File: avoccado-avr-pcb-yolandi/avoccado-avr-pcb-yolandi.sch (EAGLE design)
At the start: 36 parts, among them Q1 16MHz

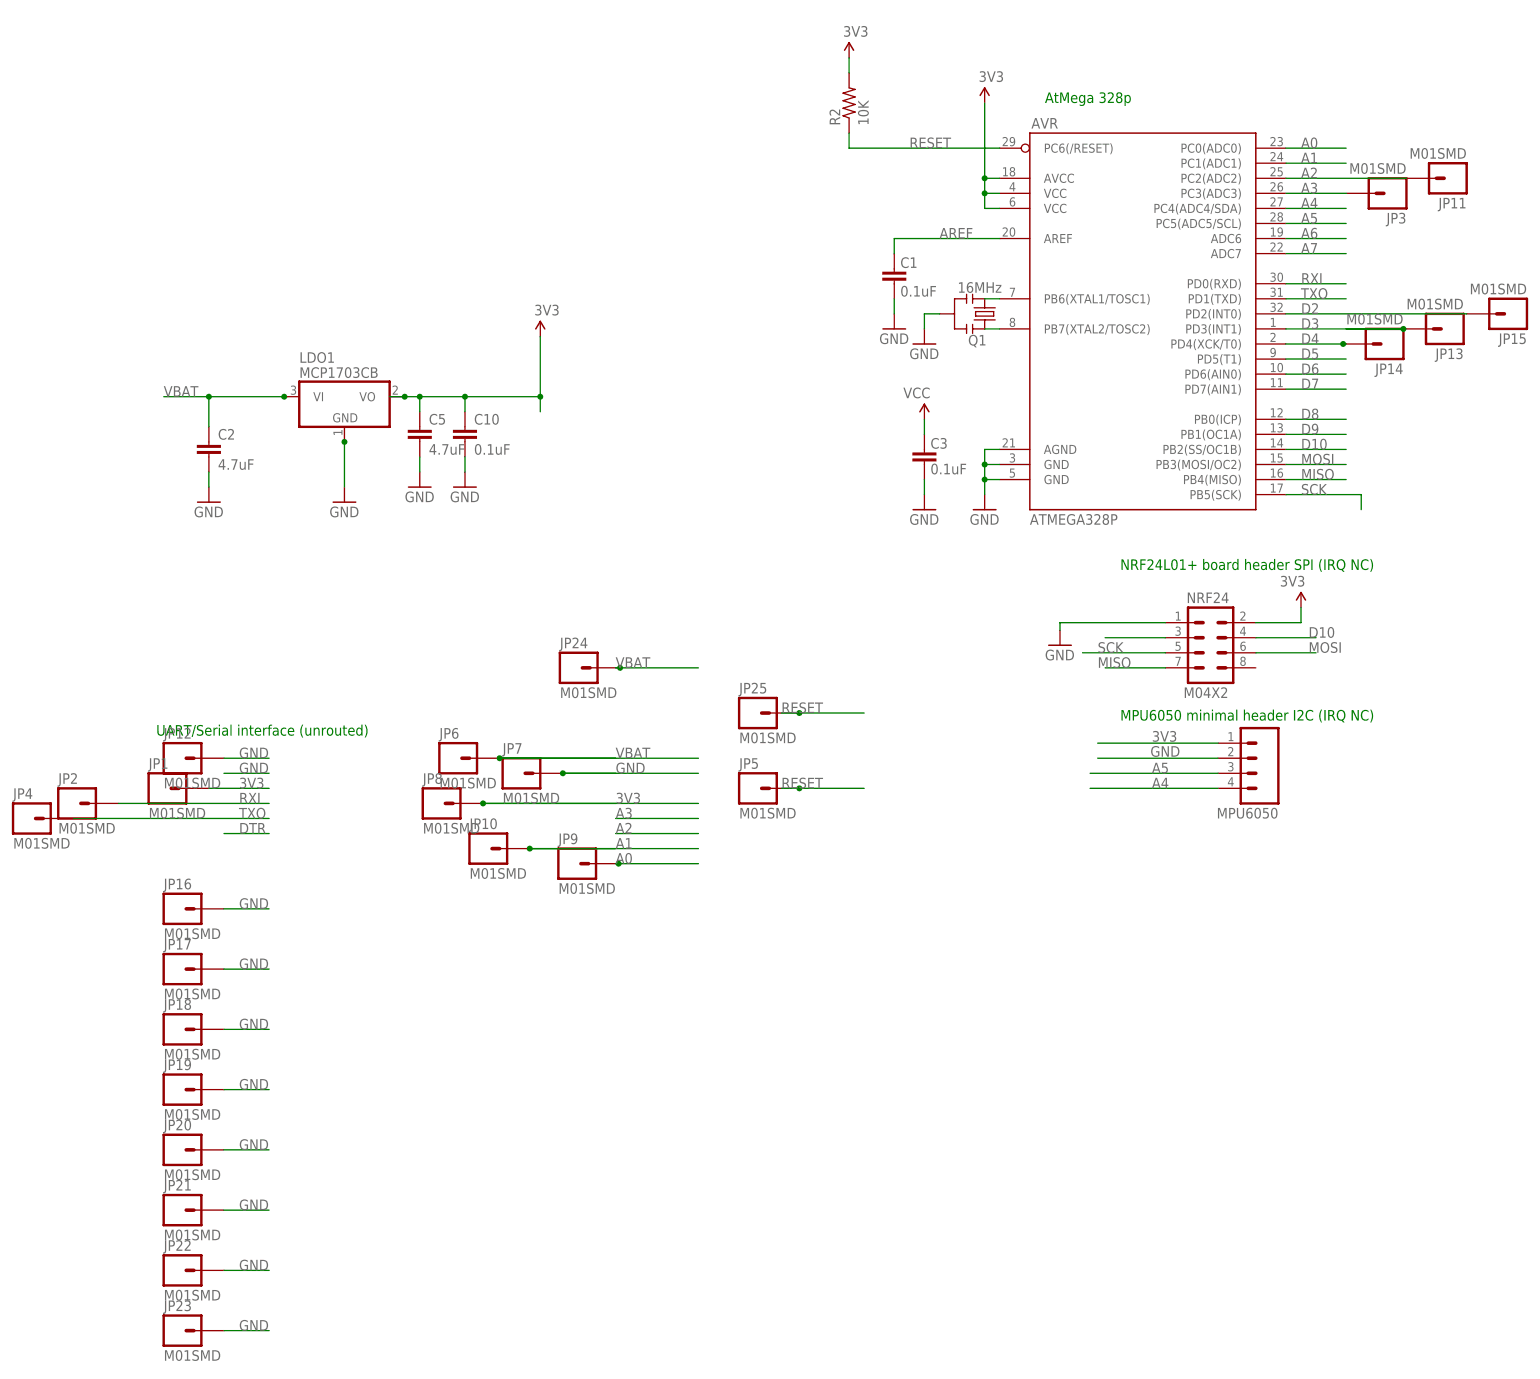
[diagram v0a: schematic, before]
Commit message: start new 1 sq inch PCB fork 'yolandi'
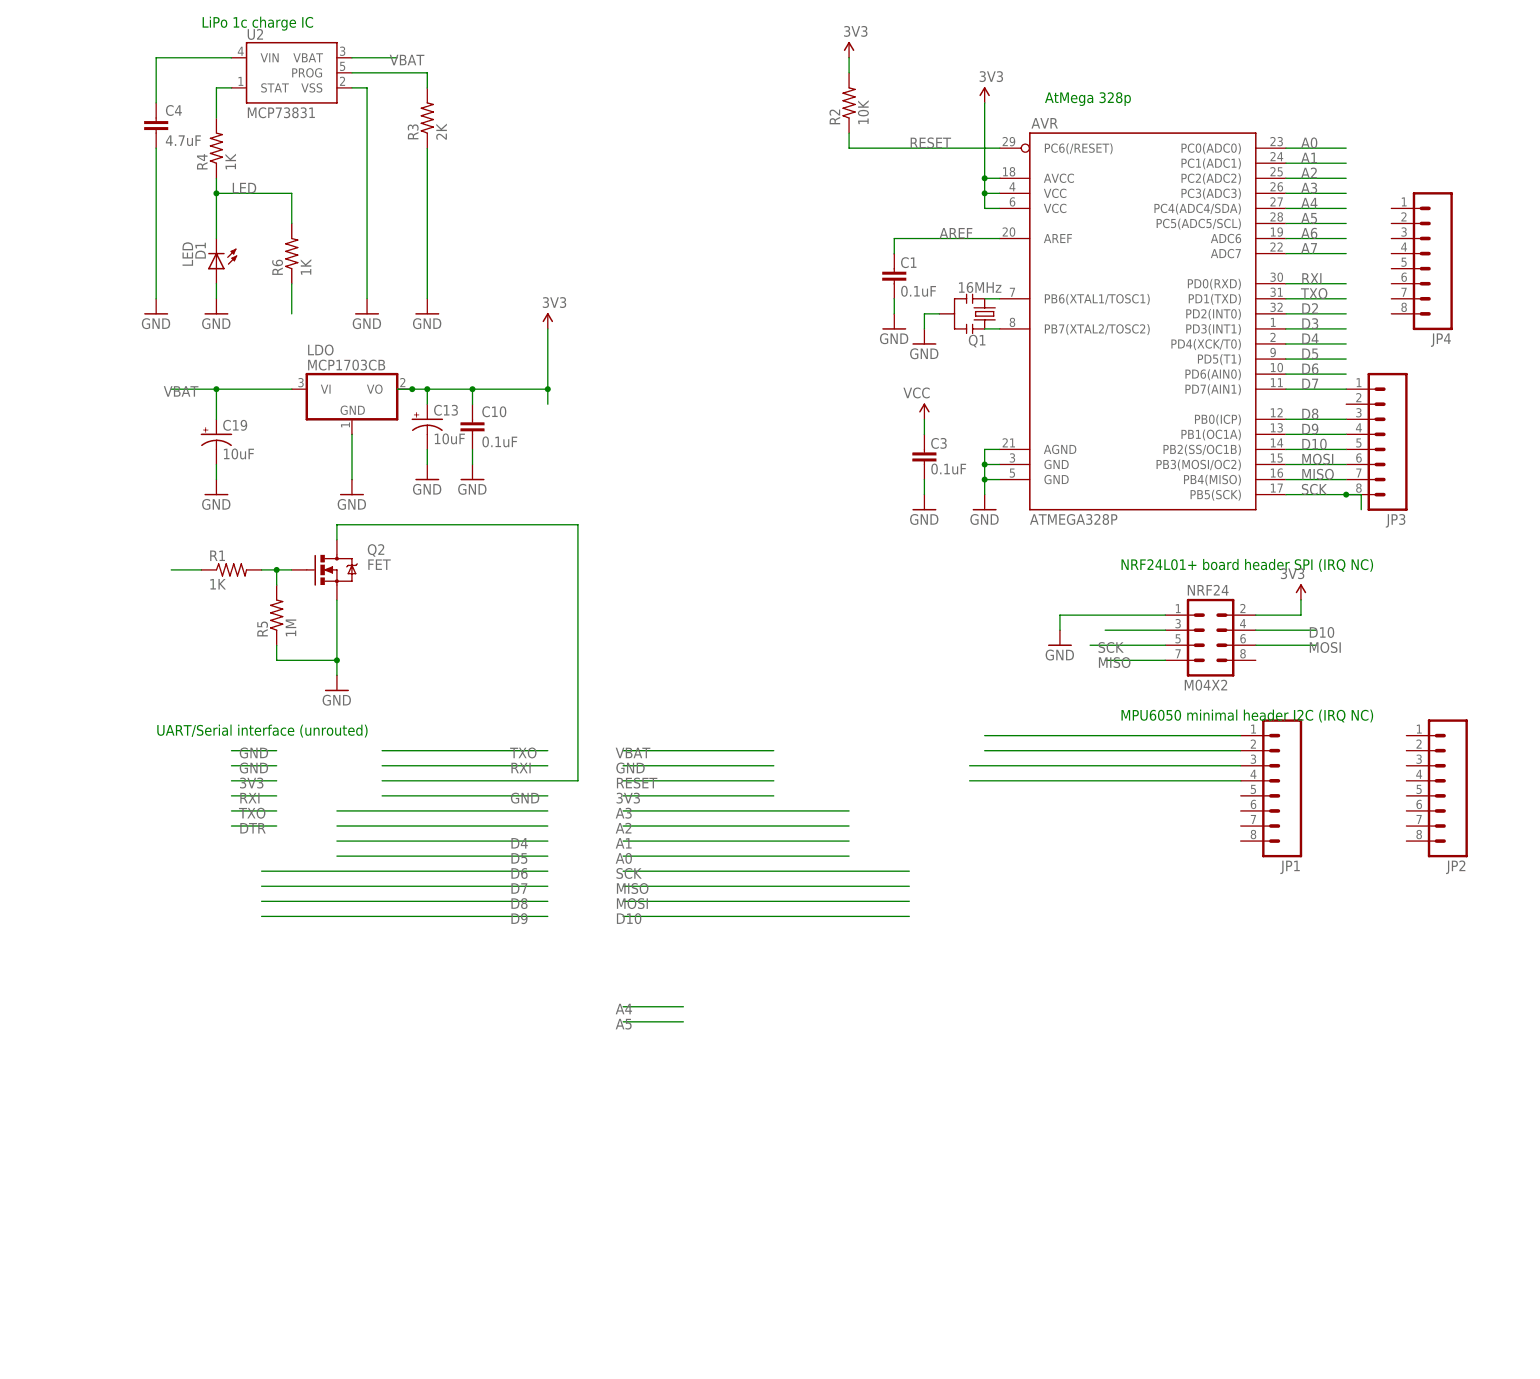
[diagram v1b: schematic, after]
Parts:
- removed C2, C5: 4.7uF, SparkFun-Capacitors:4.7UF-6.3V-10%(0603)0603
- removed JP10, JP11, JP12, JP13, JP14, JP15, JP16, JP17, JP18, JP19, JP20, JP21, JP22, JP23, JP24, JP25, JP5, JP6, JP7, JP8, JP9: M01SMD, SparkFun-Connectors:M01SMD
- removed LDO1: MCP1703CB, linear:MCP1703CB
- removed MPU6050: (no value), SparkFun-Connectors:M041X04_NO_SILK
- added C13, C19: 10uF, SparkFun:CAP_POL1206
- added C4: 4.7uF, SparkFun-Capacitors:4.7UF-6.3V-10%(0603)0603
- added D1: LED, SparkFun:LED0603
- added LDO: MCP1703CB, linear:MCP1703CB
- added Q2: FET, SparkFun-DiscreteSemi:MOSFET-NCHANNEL2N7002PW
- added R1, R4, R6: 1K, SparkFun-Resistors:RESISTOR0603
- added R3: 2K, SparkFun-Resistors:RESISTOR0603
- added R5: 1M, SparkFun-Resistors:RESISTOR0603
- added U2: MCP73831, SparkFun:MCP73831
- JP1, JP2, JP3, JP4: value M01SMD -> (none); device SparkFun-Connectors:M01SMD -> SparkFun-Connectors:M08NO_SILK
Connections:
- new net BUS: C4.1, U2.VIN
- new net LED: D1.C, R4.1, R6.2
- new net N$3: R3.2, U2.PROG
- new net N$4: R4.2, U2.STAT
- new net N$5: R6.1
- new net N$6: Q2.G, R1.2, R5.2
- new net VIBR: Q2.D
- net 3V3: now also C13.+, LDO.VO; no longer C5.1, JP8.1, LDO1.VO, MPU6050.1
- net A0: no longer JP9.1
- net A1: no longer JP10.1
- net A2: no longer JP11.1
- net A3: no longer JP3.1
- net A4: now also JP1.4; no longer MPU6050.4
- net A5: now also JP1.3; no longer MPU6050.3
- net D10: now also JP3.5
- net D2: no longer JP15.1
- net D3: now also R1.1; no longer JP13.1
- net D4: no longer JP14.1
- net D7: now also JP3.1
- net D8: now also JP3.3
- net D9: now also JP3.4
- net GND: now also C13.-, C19.-, C4.2, D1.A, JP1.2, LDO.GND, Q2.S, R3.1, R5.1, U2.VSS; no longer C2.2, C5.2, JP12.1, JP16.1, JP17.1, JP18.1, JP19.1, JP20.1, JP21.1, JP22.1, JP23.1, JP7.1, LDO1.GND, MPU6050.2
- net MISO: now also JP3.7
- net MOSI: now also JP3.6
- net RESET: no longer JP25.1, JP5.1
- net RXI: no longer JP2.1
- net SCK: now also JP3.8
- net TXO: no longer JP4.1
- net VBAT: now also C19.+, LDO.VI, U2.VBAT; no longer C2.1, JP24.1, JP6.1, LDO1.VI
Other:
- note added: "LiPo 1c charge IC"
- moved on the sheet: C10, NRF24

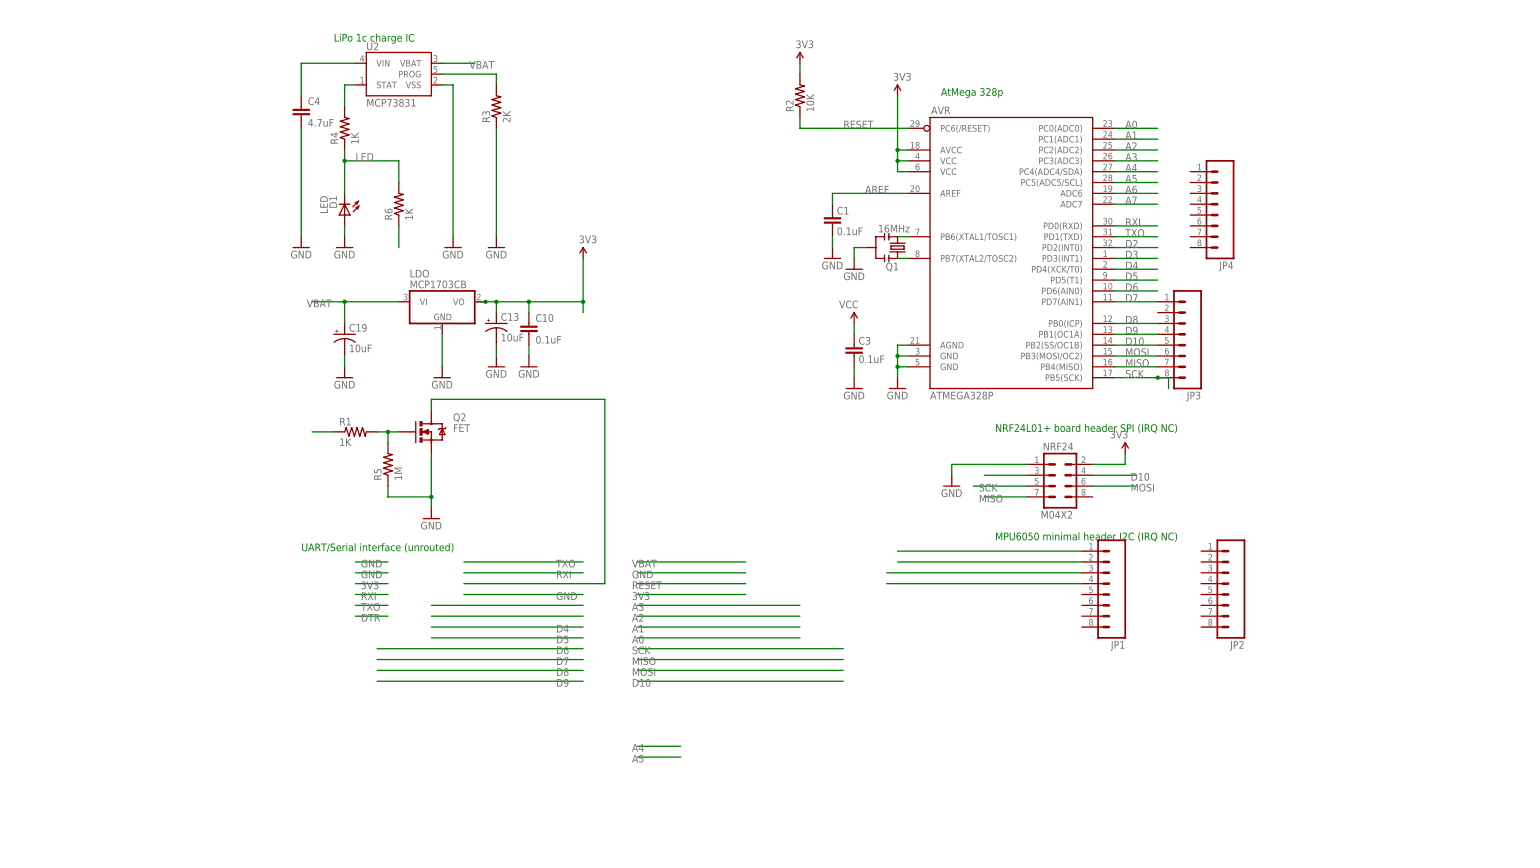
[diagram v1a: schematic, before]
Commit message: routing yolandi
added DTR-reset latch circuit with 0.1uF C
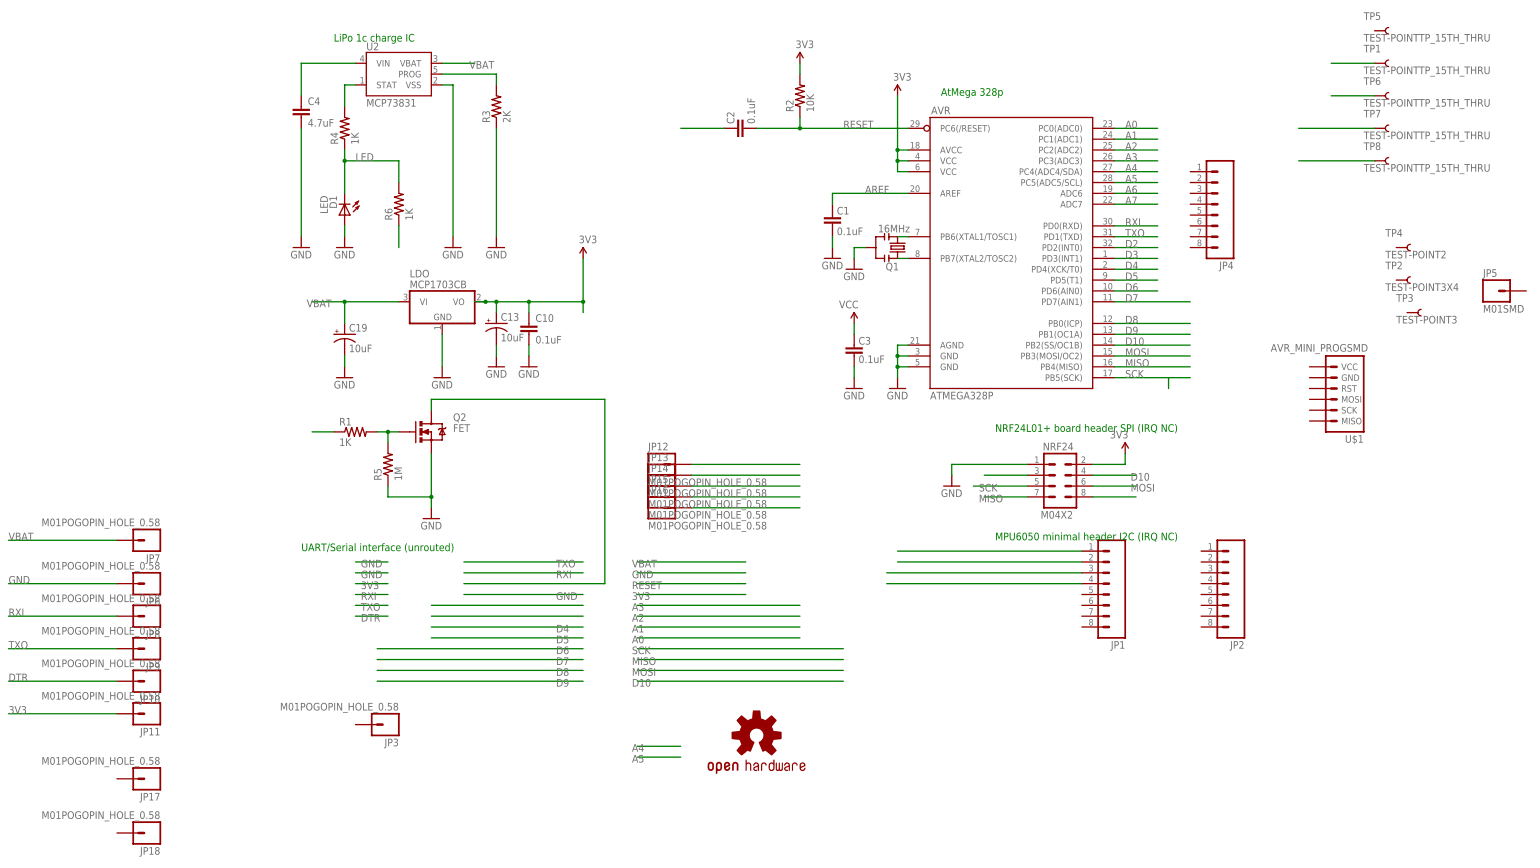
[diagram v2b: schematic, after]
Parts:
- added C2: 0.1uF, SparkFun:CAP0402
- added JP10, JP11, JP12, JP13, JP14, JP15, JP16, JP17, JP18, JP6, JP7, JP8, JP9: M01POGOPIN_HOLE_0.58, SparkFun-Connectors:M01POGOPIN_HOLE_0.58
- added JP5: M01SMD, SparkFun-Connectors:M01SMD
- added LOGO1: OSHW-LOGOS, SparkFun-Aesthetics:OSHW-LOGOS
- added TP1, TP5, TP6, TP7, TP8: TEST-POINTTP_15TH_THRU, SparkFun-Passives:TEST-POINTTP_15TH_THRU
- added TP2: TEST-POINT3X4, SparkFun-Passives:TEST-POINT3X4
- added TP3: TEST-POINT3, SparkFun-Passives:TEST-POINT3
- added TP4: TEST-POINT2, SparkFun-Passives:TEST-POINT2
- added U$1: AVR_MINI_PROGSMD, SparkFun-Connectors:AVR_MINI_PROGSMD
- JP3: value (none) -> M01POGOPIN_HOLE_0.58; device SparkFun-Connectors:M08NO_SILK -> SparkFun-Connectors:M01POGOPIN_HOLE_0.58
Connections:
- net BUS renamed 5V
- net N$3 renamed CHG-PROG
- net N$4 renamed SOC
- removed net N$5: R6.1
- new net DTR: C2.2, JP10.1
- net 3V3: now also JP11.1, JP16.1
- net A7: now also NRF24.8
- net D10: no longer JP3.5
- net D4: now also R6.1
- net D5: now also TP1.1
- net D6: now also TP6.1
- net D7: now also TP7.1; no longer JP3.1
- net D8: now also TP8.1; no longer JP3.3
- net D9: no longer JP3.4
- net GND: now also JP6.1
- net MISO: now also JP12.1; no longer JP3.7
- net MOSI: now also JP14.1; no longer JP3.6
- net RESET: now also C2.1, JP15.1
- net RXI: now also JP8.1
- net SCK: now also JP13.1; no longer JP3.8
- net TXO: now also JP9.1
- net VBAT: now also JP7.1
